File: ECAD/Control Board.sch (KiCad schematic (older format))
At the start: 63 parts, among them J3 Thermocouple, J4 SD_Card, J5 PWR/Heat, J7 UPDI, Q1 IPD50N06S4L08, SW1 Reflow, SW2 Stop, SW3 Set temp mode, U1 ATtiny1614-SS, U2 TPS7B8833QKVURQ1, U3 AD8497, U4 HT16K33

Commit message: Cleanup
Renamed files, removed temp files
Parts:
- removed D2: 1N4148, Diode_SMD:D_0805_2012Metric_Pad1.15x1.40mm_HandSolder, symbol Device:D
- removed JP1: A2, Jumper:SolderJumper-2_P1.3mm_Open_Pad1.0x1.5mm, symbol Jumper:SolderJumper_2_Open
- removed JP2: A1, Jumper:SolderJumper-2_P1.3mm_Open_Pad1.0x1.5mm, symbol Jumper:SolderJumper_2_Open
- removed JP3: A0, Jumper:SolderJumper-2_P1.3mm_Open_Pad1.0x1.5mm, symbol Jumper:SolderJumper_2_Open
- removed R25, R26, R27: 39K, Resistor_SMD:R_1206_3216Metric_Pad1.30x1.75mm_HandSolder, symbol Device:R
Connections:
- wire segments 94 -> 91
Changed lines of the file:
@@
 $Descr A4 11693 8268
 encoding utf-8
-Sheet 1 2
+Sheet 1 1
 Title "Heater Control Board"
 Date "2021-08-25"
@@
 Comment4 ""
 $EndDescr
-$Sheet
-S 6350 2500 550  300
-U 61206046
-F0 "Heater" 50
-F1 "Heater.sch" 50
-F2 "+" I L 6350 2600 50
-F3 "-" I L 6350 2700 50
-$EndSheet
 $Comp
 L power:GND #PWR0101
@@
 Text Label 2550 5550 0    50   ~ 0
 K11
-$Comp
-L Jumper:SolderJumper_2_Open JP3
-U 1 1 6143BA2B
-P 1600 7600
-F 0 "JP3" H 1600 7805 50  0000 C CNN
-F 1 "A0" H 1600 7714 50  0000 C CNN
-F 2 "Jumper:SolderJumper-2_P1.3mm_Open_Pad1.0x1.5mm" H 1600 7600 50  0001 C CNN
-F 3 "~" H 1600 7600 50  0001 C CNN
-	1    1600 7600
-	1    0    0    -1
-$EndComp
-$Comp
-L Jumper:SolderJumper_2_Open JP2
-U 1 1 61439426
-P 1600 7300
-F 0 "JP2" H 1600 7505 50  0000 C CNN
-F 1 "A1" H 1600 7414 50  0000 C CNN
-F 2 "Jumper:SolderJumper-2_P1.3mm_Open_Pad1.0x1.5mm" H 1600 7300 50  0001 C CNN
-F 3 "~" H 1600 7300 50  0001 C CNN
-	1    1600 7300
-	1    0    0    -1
-$EndComp
-$Comp
-L Jumper:SolderJumper_2_Open JP1
-U 1 1 61437829
-P 1600 7000
-F 0 "JP1" H 1600 7205 50  0000 C CNN
-F 1 "A2" H 1600 7114 50  0000 C CNN
-F 2 "Jumper:SolderJumper-2_P1.3mm_Open_Pad1.0x1.5mm" H 1600 7000 50  0001 C CNN
-F 3 "~" H 1600 7000 50  0001 C CNN
-	1    1600 7000
-	1    0    0    -1
-$EndComp
-$Comp
-L Device:D D2
-U 1 1 6145F0AE
-P 2350 7300
-F 0 "D2" H 2350 7517 50  0000 C CNN
-F 1 "1N4148" H 2350 7426 50  0000 C CNN
-F 2 "Diode_SMD:D_0805_2012Metric_Pad1.15x1.40mm_HandSolder" H 2350 7300 50  0001 C CNN
-F 3 "~" H 2350 7300 50  0001 C CNN
-	1    2350 7300
-	1    0    0    -1
-$EndComp
-Wire Wire Line
-	2050 7600 2050 7300
-Connection ~ 2050 7300
-Wire Wire Line
-	2050 7300 2050 7000
-Wire Wire Line
-	2050 7300 2200 7300
-Text Label 2500 7300 0    50   ~ 0
-COM1
-$Comp
-L Device:R R25
-U 1 1 61470E24
-P 1900 7000
-F 0 "R25" V 1800 7000 50  0000 C CNN
-F 1 "39K" V 1900 7000 50  0000 C CNN
-F 2 "Resistor_SMD:R_1206_3216Metric_Pad1.30x1.75mm_HandSolder" V 1830 7000 50  0001 C CNN
-F 3 "~" H 1900 7000 50  0001 C CNN
-	1    1900 7000
-	0    1    1    0
-$EndComp
-$Comp
-L Device:R R26
-U 1 1 61471F8C
-P 1900 7300
-F 0 "R26" V 1800 7300 50  0000 C CNN
-F 1 "39K" V 1900 7300 50  0000 C CNN
-F 2 "Resistor_SMD:R_1206_3216Metric_Pad1.30x1.75mm_HandSolder" V 1830 7300 50  0001 C CNN
-F 3 "~" H 1900 7300 50  0001 C CNN
-	1    1900 7300
-	0    1    1    0
-$EndComp
-$Comp
-L Device:R R27
-U 1 1 6147468E
-P 1900 7600
-F 0 "R27" V 1800 7600 50  0000 C CNN
-F 1 "39K" V 1900 7600 50  0000 C CNN
-F 2 "Resistor_SMD:R_1206_3216Metric_Pad1.30x1.75mm_HandSolder" V 1830 7600 50  0001 C CNN
-F 3 "~" H 1900 7600 50  0001 C CNN
-	1    1900 7600
-	0    1    1    0
-$EndComp
-Text Label 1450 7000 2    50   ~ 0
-A2Add
-Text Label 1450 7300 2    50   ~ 0
-A1Add
-Text Label 1450 7600 2    50   ~ 0
-A0Add
 Text Label 5100 4400 2    50   ~ 0
 K1

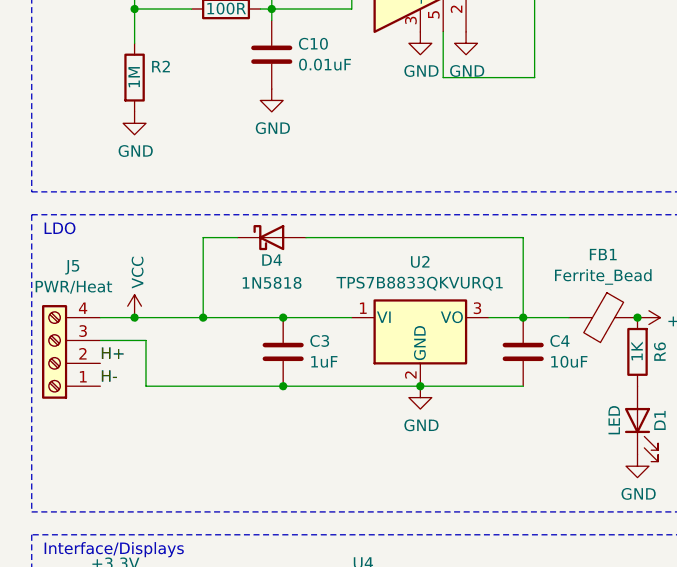
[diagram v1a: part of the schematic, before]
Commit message: High voltage modifications
Widened high voltage tracks and replaced schottky diode with higher back voltage diode.
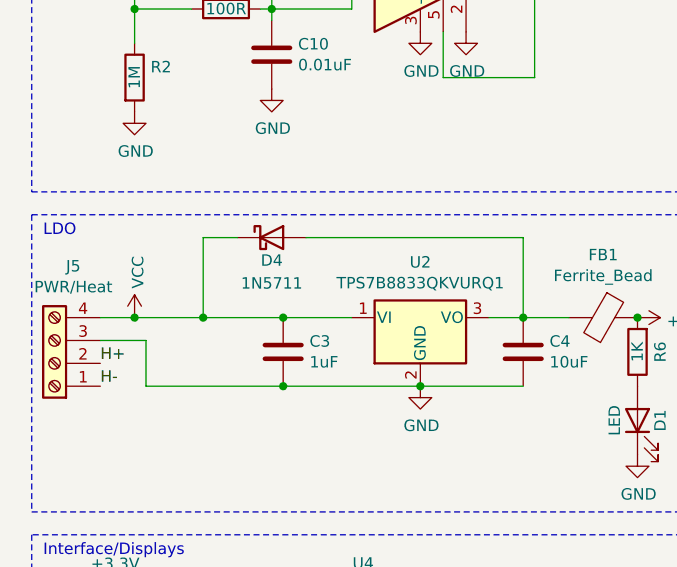
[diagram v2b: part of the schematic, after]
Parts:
- D4: value 1N5818 -> 1N5711
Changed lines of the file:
@@
 P 1550 2600
 F 0 "D4" H 1550 2500 50  0000 C CNN
-F 1 "1N5818" H 1550 2400 50  0000 C CNN
+F 1 "1N5711" H 1550 2400 50  0000 C CNN
 F 2 "Diode_THT:D_T-1_P5.08mm_Horizontal" H 1550 2600 50  0001 C CNN
 F 3 "~" H 1550 2600 50  0001 C CNN

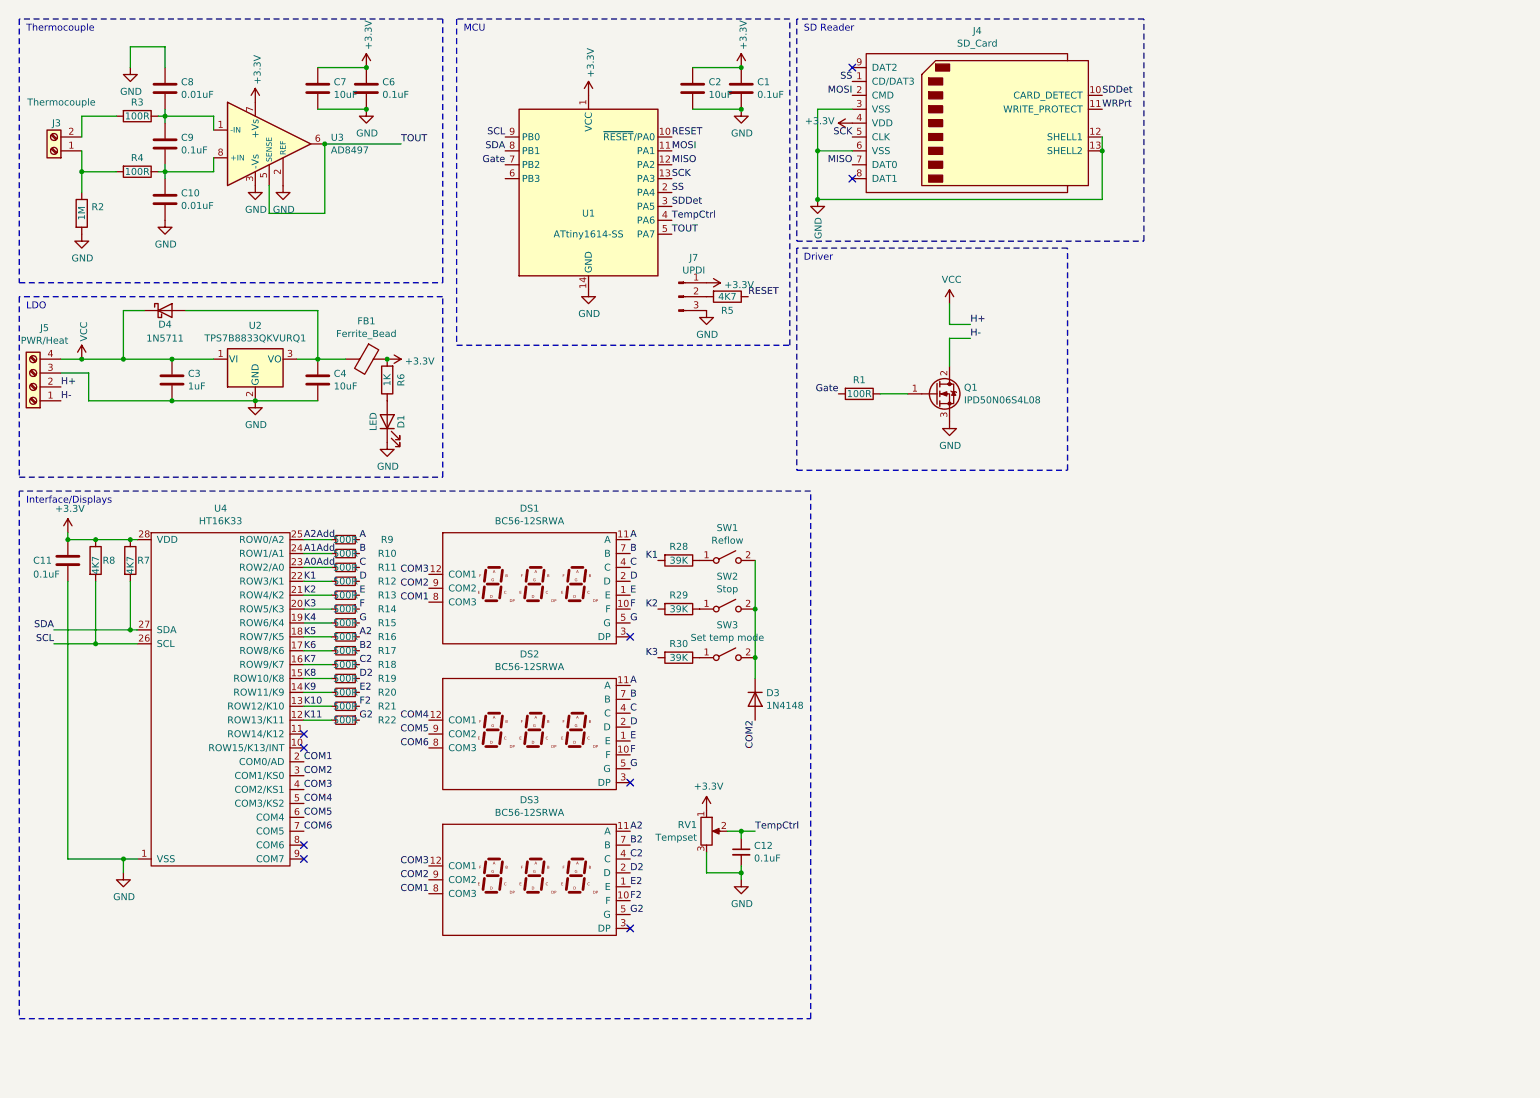
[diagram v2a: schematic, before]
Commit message: Revised control board schematic
Replaced single LDO setup with cascaded LDOs, so that a higher input voltage can be used, and the intermediate 12V can be used to power a fan. Added the appropriate circuitry to control a fan. Added test points for each voltage level and ground.

Layout is still to be updated
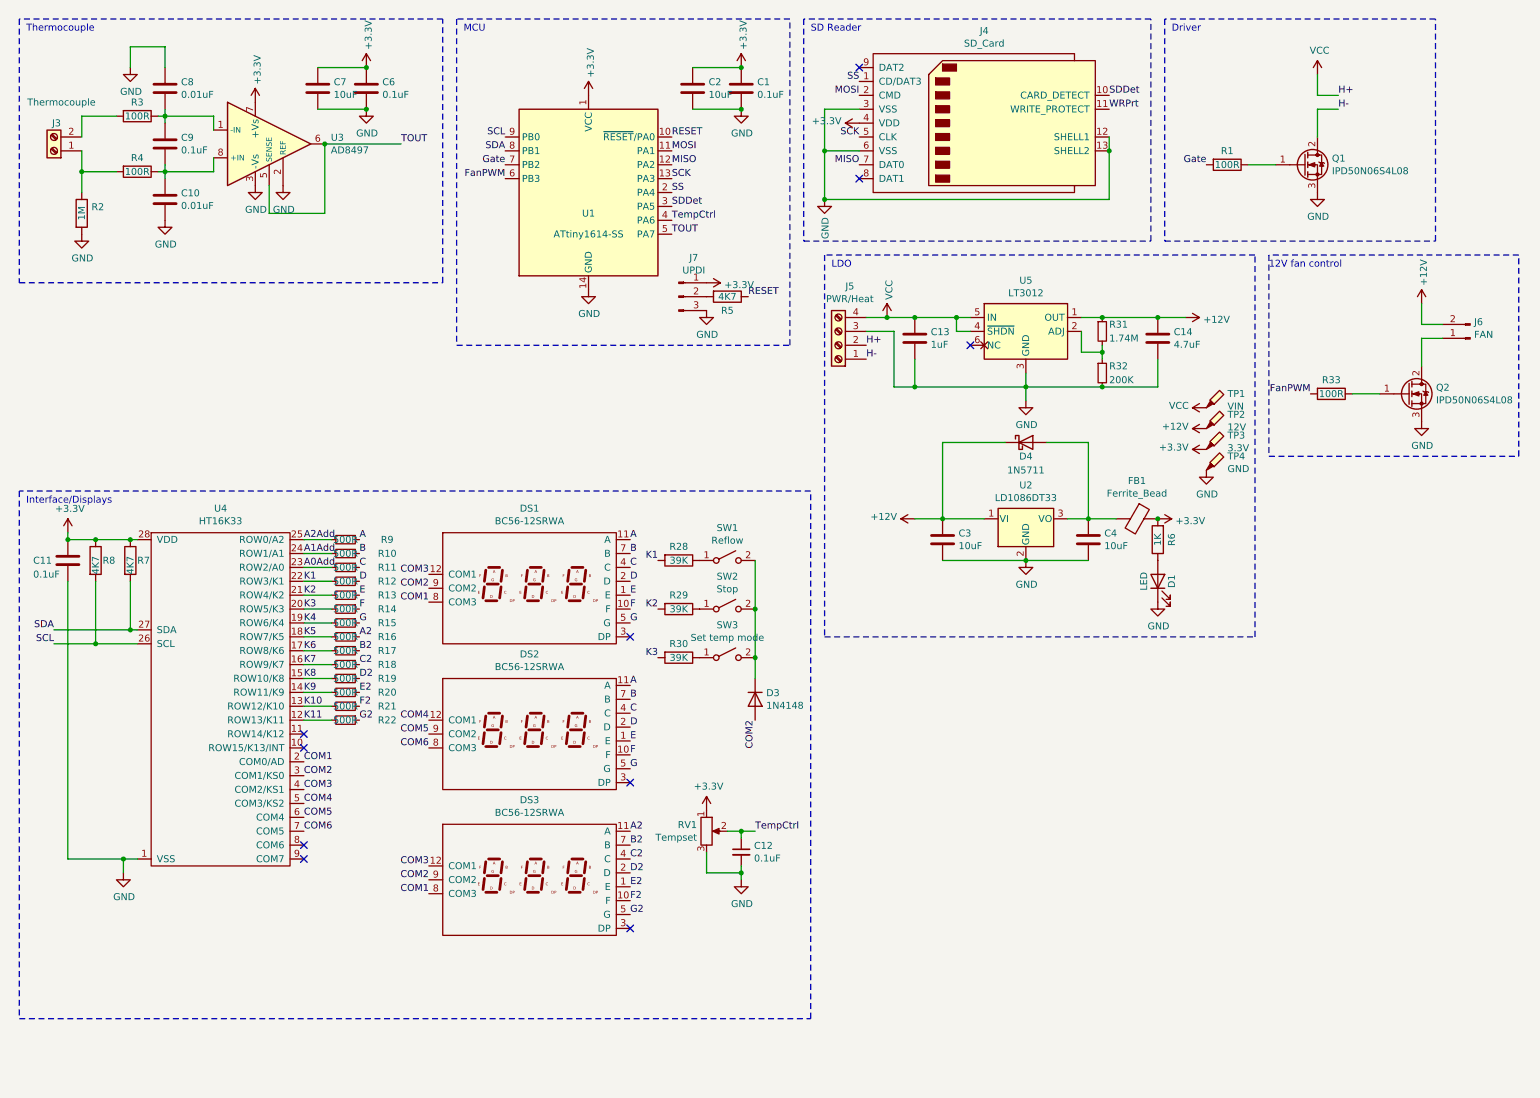
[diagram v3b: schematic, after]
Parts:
- added C13: 1uF, Capacitor_SMD:C_0805_2012Metric_Pad1.18x1.45mm_HandSolder, symbol Device:C
- added C14: 4.7uF, Capacitor_SMD:C_0805_2012Metric_Pad1.18x1.45mm_HandSolder, symbol Device:C
- added J6: FAN, symbol Connector:Conn_01x02_Male
- added Q2: IPD50N06S4L08, Package_TO_SOT_SMD:TO-252-2, symbol Transistor_FET:IPD50R380CE
- added R31: 1.74M, Resistor_SMD:R_0805_2012Metric_Pad1.20x1.40mm_HandSolder, symbol Device:R_Small
- added R32: 200K, Resistor_SMD:R_0805_2012Metric_Pad1.20x1.40mm_HandSolder, symbol Device:R_Small
- added R33: 100R, Resistor_SMD:R_1206_3216Metric_Pad1.30x1.75mm_HandSolder, symbol Device:R
- added TP1: VIN, TestPoint:TestPoint_Pad_3.0x3.0mm, symbol Connector:TestPoint_Probe
- added TP2: 12V, TestPoint:TestPoint_Pad_3.0x3.0mm, symbol Connector:TestPoint_Probe
- added TP3: 3.3V, TestPoint:TestPoint_Pad_3.0x3.0mm, symbol Connector:TestPoint_Probe
- added TP4: GND, TestPoint:TestPoint_Pad_3.0x3.0mm, symbol Connector:TestPoint_Probe
- added U5: LT3012, symbol Regulators:LT3012
- C3: value 1uF -> 10uF
- U2: value TPS7B8833QKVURQ1 -> LD1086DT33
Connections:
- net +3V3: now also TP3.1
- net GND: now also C13.2, C14.2, Q2.3 (S), R32.2, TP4.1, U5.3 (GND)
- net VCC: now also C13.1, TP1.1, U5.4 (~SHDN), U5.5 (IN); no longer C3.1, D4.1 (K), U2.1 (VI)
- net FanPWM: now reaches U1.6 (PB3)
- net FanPWM: now also R33.2
- new net: R31.2, R32.1, U5.2 (ADJ)
- new net: Q2.1 (G), R33.1
- new net: J6.1 (Pin_1), Q2.2 (D)
- new net +12V: C14.1, C3.1, D4.1 (K), J6.2 (Pin_2), R31.1, TP2.1, U2.1 (VI), U5.1 (OUT)
- no-connect marks 9 -> 10
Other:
- note added: "12V fan control"
- moved on the sheet: C3, C4, D1, D4, FB1, J4, J5, Q1, R1, R6, U2

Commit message: Added footprints to board
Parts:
- J6: footprint (none) -> Connector_PinHeader_2.54mm:PinHeader_1x02_P2.54mm_Vertical
- U5: footprint (none) -> PCB Heater:Linear_Technology-LT3012EFETRPBF-Level_B
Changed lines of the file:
@@
 F 0 "U5" H 7750 3117 50  0000 C CNN
 F 1 "LT3012" H 7750 3026 50  0000 C CNN
-F 2 "" H 7750 3075 50  0001 C CNN
+F 2 "PCB Heater:Linear_Technology-LT3012EFETRPBF-Level_B" H 7750 3075 50  0001 C CNN
 F 3 "" H 7750 2750 50  0001 C CNN
 	1    7750 2750
@@
 FanPWM
 $Comp
-L power:GND #PWR?
+L power:GND #PWR0134
 U 1 1 6146C500
 P 10600 3400
-F 0 "#PWR?" H 10600 3150 50  0001 C CNN
+F 0 "#PWR0134" H 10600 3150 50  0001 C CNN
 F 1 "GND" H 10605 3227 50  0000 C CNN
 F 2 "" H 10600 3400 50  0001 C CNN
@@
 	10600 2800 10600 3000
 $Comp
-L power:+12V #PWR?
+L power:+12V #PWR0135
 U 1 1 6147371F
 P 10600 2550
-F 0 "#PWR?" H 10600 2400 50  0001 C CNN
+F 0 "#PWR0135" H 10600 2400 50  0001 C CNN
 F 1 "+12V" V 10615 2678 50  0000 L CNN
 F 2 "" H 10600 2550 50  0001 C CNN
@@
 F 0 "J6" H 10922 2682 50  0000 R CNN
 F 1 "FAN" H 10922 2773 50  0000 R CNN
-F 2 "" H 10950 2800 50  0001 C CNN
+F 2 "Connector_PinHeader_2.54mm:PinHeader_1x02_P2.54mm_Vertical" H 10950 2800 50  0001 C CNN
 F 3 "~" H 10950 2800 50  0001 C CNN
 	1    10950 2800

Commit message: Re-arrange components
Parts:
- TP1, TP2, TP3, TP4: footprint TestPoint:TestPoint_Pad_3.0x3.0mm -> TestPoint:TestPoint_Pad_2.0x2.0mm
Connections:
- net GND: now also J5.1 (Pin_1); no longer J5.3 (Pin_3)
- net H-: now also J5.2 (Pin_2); no longer J5.1 (Pin_1)
- net VCC: now also J5.3 (Pin_3); no longer J5.2 (Pin_2)
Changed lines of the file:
@@
 $EndComp
 Wire Wire Line
-	6600 2750 6800 2750
+	6600 2950 6800 2950
+Text Label 6600 2750 0    50   ~ 0
+H+
 Text Label 6600 2850 0    50   ~ 0
-H+
-Text Label 6600 2950 0    50   ~ 0
 H-
 $Comp
@@
 	8300 3150 7750 3150
 Wire Wire Line
-	6800 2750 6800 3150
-Wire Wire Line
 	8300 3150 8700 3150
 Wire Wire Line
@@
 F 0 "TP1" H 9202 3401 50  0000 L CNN
 F 1 "VIN" H 9202 3310 50  0000 L CNN
-F 2 "TestPoint:TestPoint_Pad_3.0x3.0mm" H 9250 3300 50  0001 C CNN
+F 2 "TestPoint:TestPoint_Pad_2.0x2.0mm" H 9250 3300 50  0001 C CNN
 F 3 "~" H 9250 3300 50  0001 C CNN
 	1    9050 3300
@@
 F 0 "TP2" H 9202 3551 50  0000 L CNN
 F 1 "12V" H 9202 3460 50  0000 L CNN
-F 2 "TestPoint:TestPoint_Pad_3.0x3.0mm" H 9250 3450 50  0001 C CNN
+F 2 "TestPoint:TestPoint_Pad_2.0x2.0mm" H 9250 3450 50  0001 C CNN
 F 3 "~" H 9250 3450 50  0001 C CNN
 	1    9050 3450
@@
 F 0 "TP3" H 9202 3701 50  0000 L CNN
 F 1 "3.3V" H 9202 3610 50  0000 L CNN
-F 2 "TestPoint:TestPoint_Pad_3.0x3.0mm" H 9250 3600 50  0001 C CNN
+F 2 "TestPoint:TestPoint_Pad_2.0x2.0mm" H 9250 3600 50  0001 C CNN
 F 3 "~" H 9250 3600 50  0001 C CNN
 	1    9050 3600
@@
 F 0 "TP4" H 9202 3851 50  0000 L CNN
 F 1 "GND" H 9202 3760 50  0000 L CNN
-F 2 "TestPoint:TestPoint_Pad_3.0x3.0mm" H 9250 3750 50  0001 C CNN
+F 2 "TestPoint:TestPoint_Pad_2.0x2.0mm" H 9250 3750 50  0001 C CNN
 F 3 "~" H 9250 3750 50  0001 C CNN
 	1    9050 3750
@@
 Text Label 4000 1650 2    50   ~ 0
 FanPWM
+Wire Wire Line
+	6800 2950 6800 3150
 $EndSCHEMATC

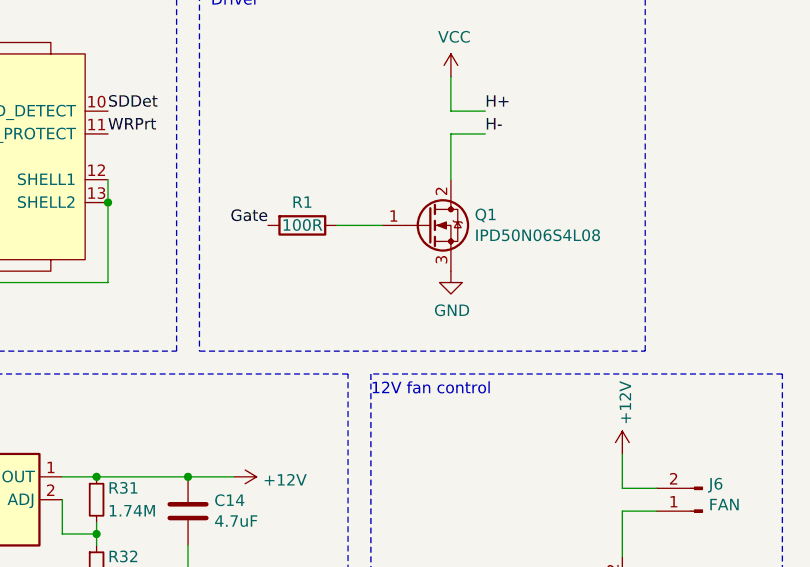
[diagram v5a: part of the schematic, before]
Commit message: Added pulldown to mosfet gate
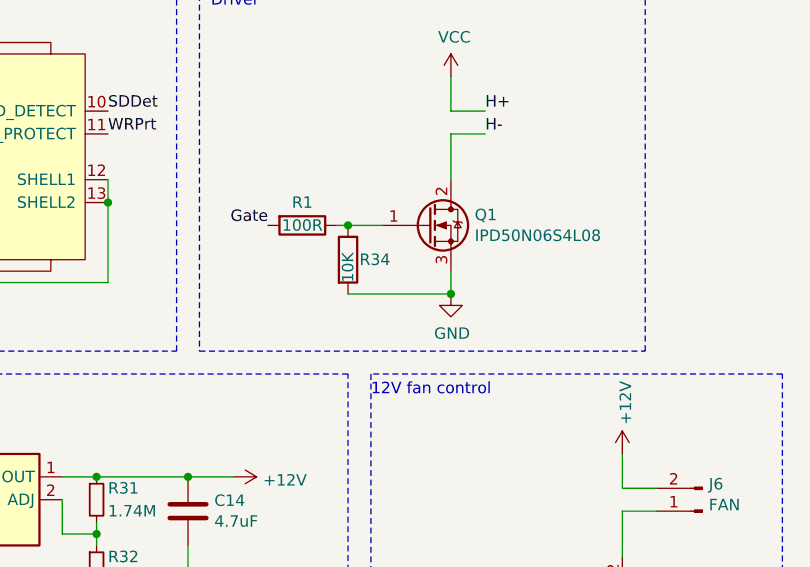
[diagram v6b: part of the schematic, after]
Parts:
- added R34: 10K, Resistor_SMD:R_1206_3216Metric_Pad1.30x1.75mm_HandSolder, symbol Device:R
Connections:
- net GND: now also R34.2
- net at Q1.1 (G), R1.1: now also R34.1
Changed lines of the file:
@@
 $EndComp
 Wire Wire Line
-	9550 1550 9350 1550
+	9550 1550 9400 1550
 $Comp
 L Device:R R1
@@
 L power:GND #PWR0103
 U 1 1 61229806
-P 9850 1750
-F 0 "#PWR0103" H 9850 1500 50  0001 C CNN
-F 1 "GND" H 9855 1577 50  0000 C CNN
-F 2 "" H 9850 1750 50  0001 C CNN
-F 3 "" H 9850 1750 50  0001 C CNN
-	1    9850 1750
+P 9850 1850
+F 0 "#PWR0103" H 9850 1600 50  0001 C CNN
+F 1 "GND" H 9855 1677 50  0000 C CNN
+F 2 "" H 9850 1850 50  0001 C CNN
+F 3 "" H 9850 1850 50  0001 C CNN
+	1    9850 1850
 	1    0    0    -1
 $EndComp
@@
 Wire Wire Line
 	6800 2950 6800 3150
+$Comp
+L Device:R R34
+U 1 1 613C7889
+P 9400 1700
+F 0 "R34" H 9450 1700 50  0000 L CNN
+F 1 "10K" V 9400 1600 50  0000 L CNN
+F 2 "Resistor_SMD:R_1206_3216Metric_Pad1.30x1.75mm_HandSolder" V 9330 1700 50  0001 C CNN
+F 3 "~" H 9400 1700 50  0001 C CNN
+	1    9400 1700
+	1    0    0    -1
+$EndComp
+Connection ~ 9400 1550
+Wire Wire Line
+	9400 1550 9350 1550
+Wire Wire Line
+	9400 1850 9850 1850
+Wire Wire Line
+	9850 1850 9850 1750
+Connection ~ 9850 1850
 $EndSCHEMATC
